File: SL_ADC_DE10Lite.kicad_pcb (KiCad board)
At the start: 4 copper layers, 98 x 67 mm, 33 parts, among them J1 DE10Lite header, J2 Conn_02x14_Odd_Even

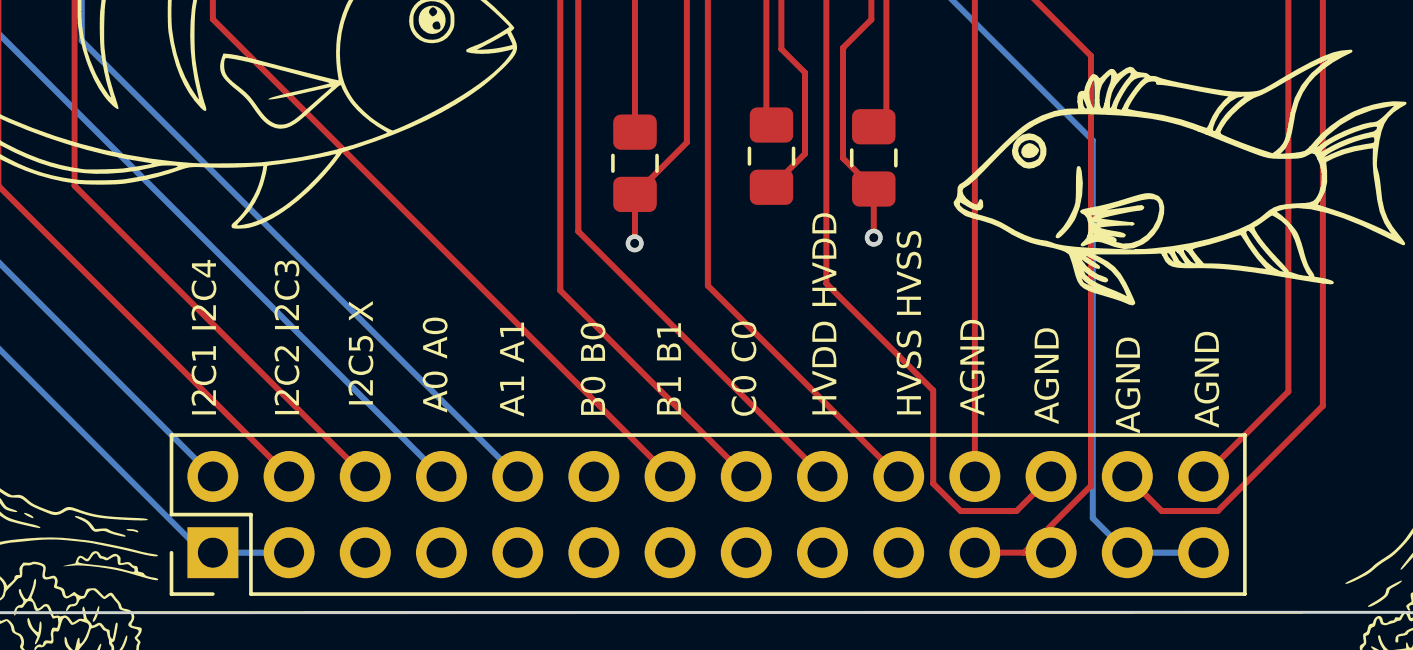
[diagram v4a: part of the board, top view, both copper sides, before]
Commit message: renamed pin silkscreens
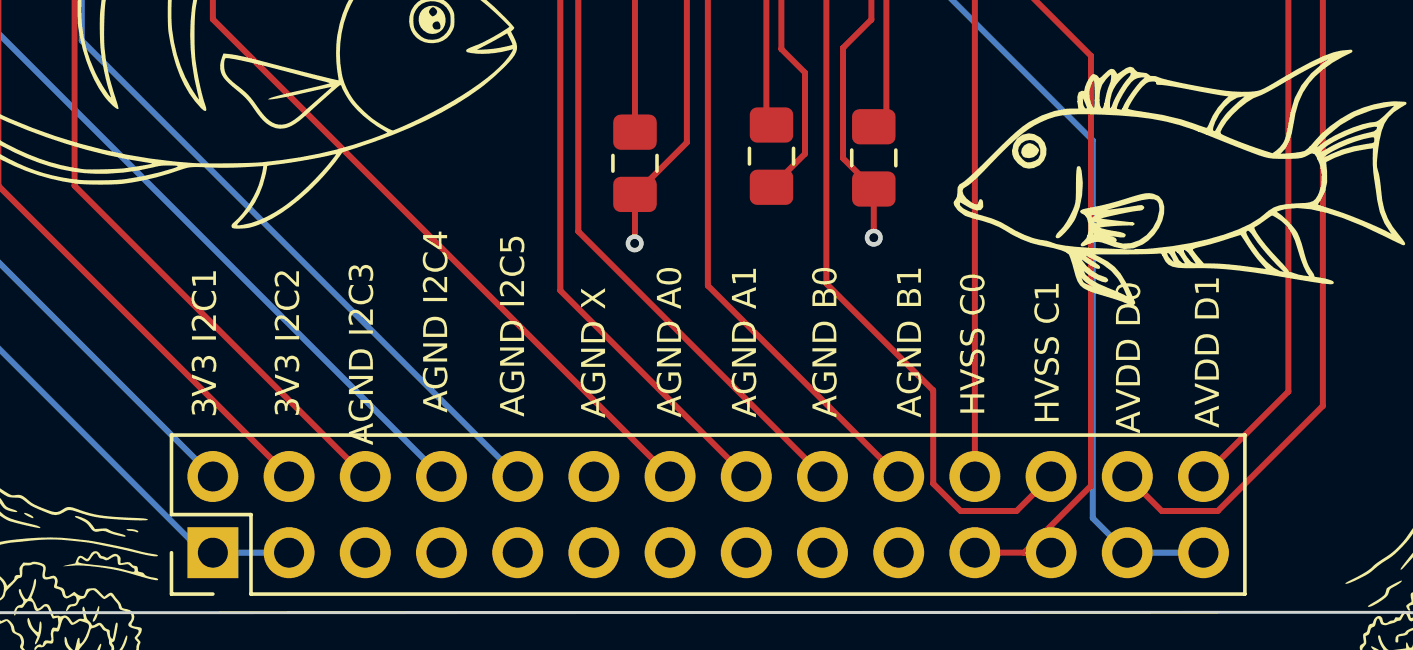
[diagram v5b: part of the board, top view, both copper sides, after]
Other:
- board text added: "3V3 I2C1"
- board text added: "3V3 I2C2"
- board text added: "AGND A0"
- board text added: "AGND A1"
- board text added: "AGND B0"
- board text added: "AGND B1"
- board text added: "AGND I2C3"
- board text added: "AGND I2C4"
- board text added: "AGND I2C5"
- board text added: "AGND X"
- board text added: "AVDD D0"
- board text added: "AVDD D1"
- board text added: "HVSS C0"
- board text added: "HVSS C1"
- board text removed: "A0 A0"
- board text removed: "A1 A1"
- board text removed: "AGND"
- board text removed: "B0 B0"
- board text removed: "B1 B1"
- board text removed: "C0 C0"
- board text removed: "HVDD HVDD"
- board text removed: "HVSS HVSS"
- board text removed: "I2C1 I2C4"
- board text removed: "I2C5 X"
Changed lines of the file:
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@@
 		)
 	)
-	(gr_text "I2C1 I2C4\n"
+	(gr_text "3V3 I2C1\n"
 		(at 93 99.5 90)
 		(layer "F.SilkS")
@@
 		)
 	)
-	(gr_text "I2C2 I2C3"
+	(gr_text "3V3 I2C2"
 		(at 95.7676 99.491457 90)
 		(layer "F.SilkS")
@@
 		)
 	)
-	(gr_text "A0 A0"
+	(gr_text "AGND I2C4"
 		(at 100.706329 99.337012 90)
 		(layer "F.SilkS")
@@
 		)
 	)
-	(gr_text "A1 A1"
+	(gr_text "AGND I2C5"
 		(at 103.269921 99.474102 90)
 		(layer "F.SilkS")
@@
 		)
 	)
-	(gr_text "B0 B0"
+	(gr_text "AGND X"
 		(at 105.970602 99.515229 90)
 		(layer "F.SilkS")
@@
 		)
 	)
-	(gr_text "B1 B1"
+	(gr_text "AGND A0"
 		(at 108.5 99.5 90)
 		(layer "F.SilkS")
@@
 		)
 	)
-	(gr_text "C0 C0"
+	(gr_text "AGND A1"
 		(at 111 99.5 90)
 		(layer "F.SilkS")
@@
 		)
 	)
-	(gr_text "HVDD HVDD"
+	(gr_text "AGND B0"
 		(at 113.680724 99.5 90)
 		(layer "F.SilkS")
@@
 		)
 	)
-	(gr_text "HVSS HVSS"
+	(gr_text "AGND B1"
 		(at 116.5 99.5 90)
 		(layer "F.SilkS")
@@
 		)
 	)
-	(gr_text "AGND"
+	(gr_text "HVSS C0"
 		(at 118.61 99.44 90)
 		(layer "F.SilkS")
@@
 		)
 	)
-	(gr_text "AGND"
+	(gr_text "HVSS C1"
 		(at 121.09 99.72 90)
 		(layer "F.SilkS")
@@
 		)
 	)
-	(gr_text "AGND"
+	(gr_text "AVDD D0"
 		(at 123.8 100.03 90)
 		(layer "F.SilkS")
@@
 		)
 	)
-	(gr_text "AGND"
+	(gr_text "AVDD D1"
 		(at 126.43 99.84 90)
 		(layer "F.SilkS")
@@
 		)
 	)
-	(gr_text "I2C5 X"
+	(gr_text "AGND I2C3"
 		(at 98.231809 97.370629 90)
 		(layer "F.SilkS")
